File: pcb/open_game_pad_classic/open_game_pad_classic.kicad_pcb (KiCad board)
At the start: 2 copper layers, 140 x 71 mm, 55 parts, among them J1 COM-09032, J2 COM-09032

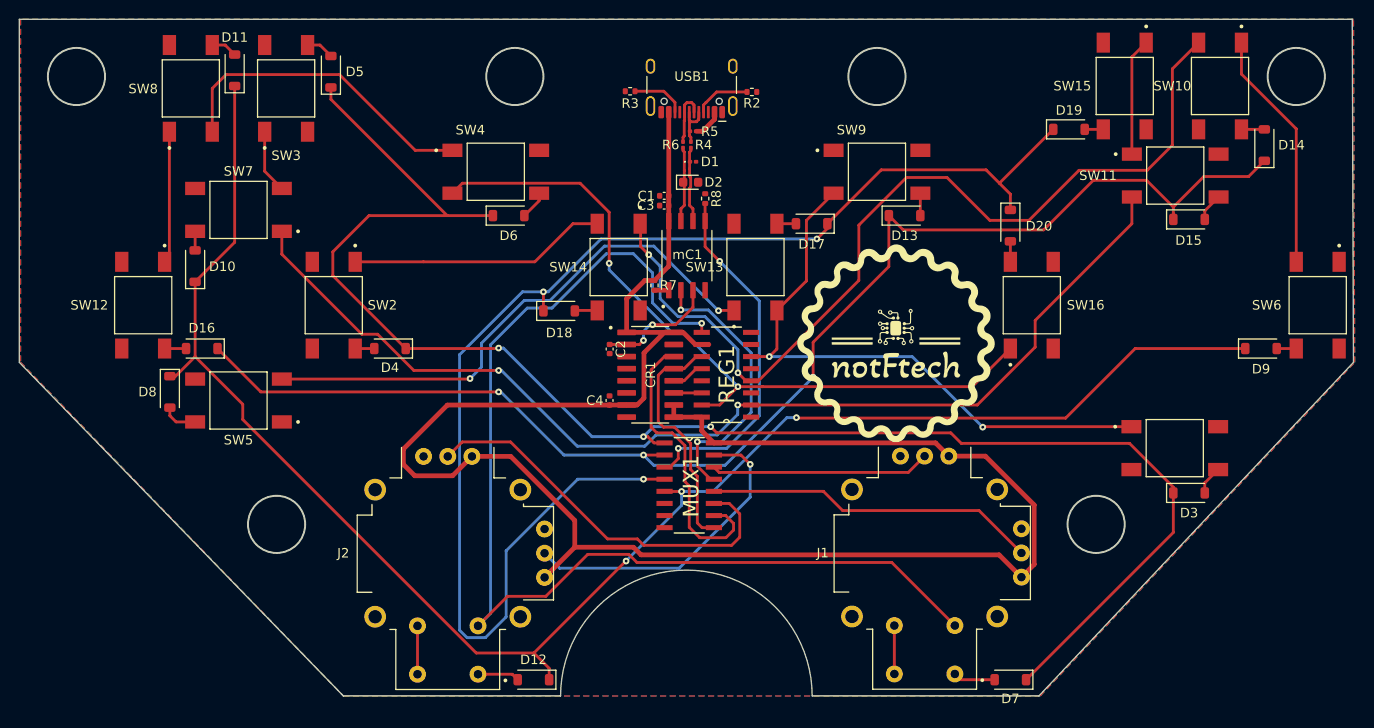
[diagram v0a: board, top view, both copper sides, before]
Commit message: Fixed the switches connections and remade the tracks in pcb.
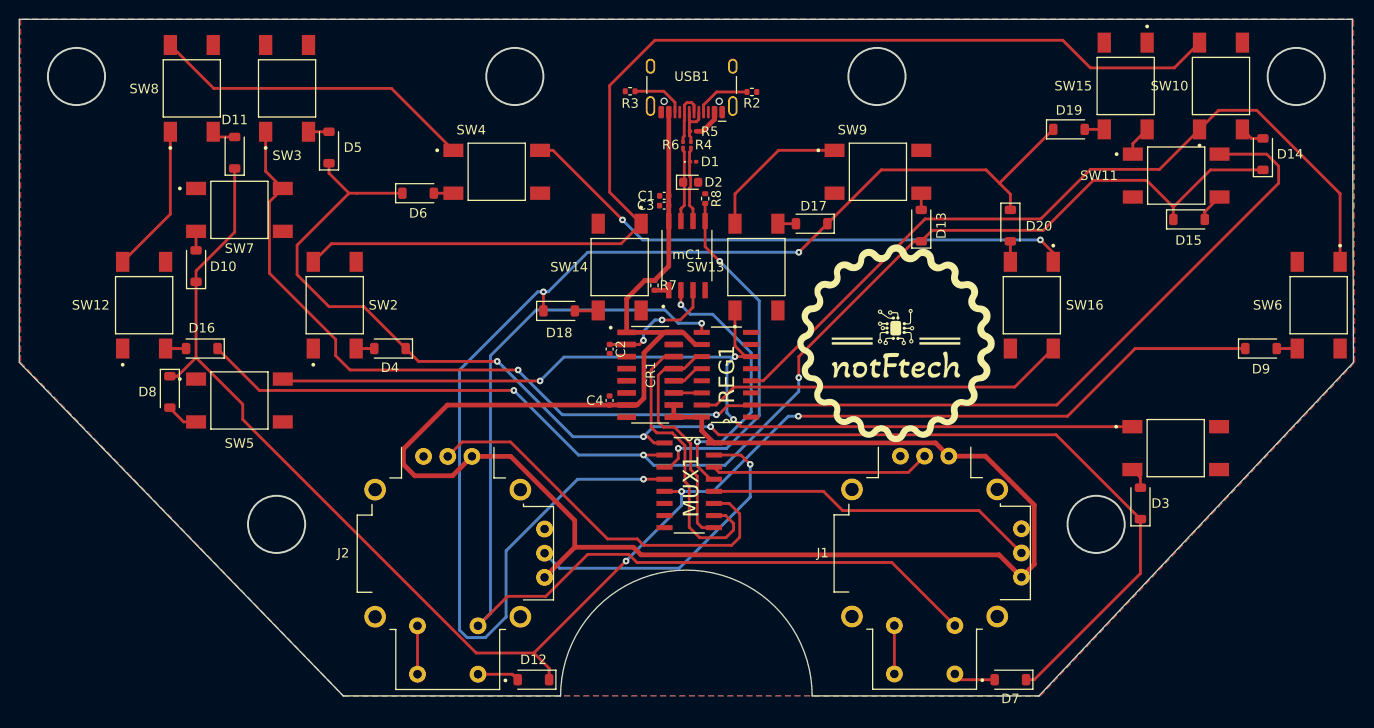
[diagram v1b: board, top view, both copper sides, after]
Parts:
- SW1: value ~ -> TS04-66-95-BK-100-SMT
- moved D6 9.79 mm to (116.8, 72.2)
- moved D11 8.65 mm to (97.6, 68.0)
- moved D5 7.95 mm to (107.5, 67.5)
- moved D3 5.22 mm to (192.7, 104.8), turned to 90 degrees
- moved D13 2.04 mm to (169.7, 75.7), turned to 90 degrees
- moved D14 0.96 mm to (205.5, 68.2)
- moved D10 0.10 mm to (93.5, 79.9)
- moved SW1 0.10 mm to (196.3, 99.0)
- moved SW10 0.10 mm to (201.1, 61.0), turned to 90 degrees
- moved SW11 0.10 mm to (196.4, 70.4)
- moved SW12 0.10 mm to (88.1, 84.0), turned to 90 degrees
- moved SW13 0.10 mm to (152.3, 80.0)
- moved SW14 0.10 mm to (138.0, 80.0)
- moved SW15 0.10 mm to (191.1, 61.0)
- moved SW2 0.10 mm to (108.1, 84.0), turned to 90 degrees
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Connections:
- SW1 pad 2: /Y4 -> Net-(D3-A)
- SW1 pad 3: Net-(D3-A) -> /Y4
- SW10 pad 2: /Y3 -> Net-(D14-A)
- SW10 pad 3: Net-(D14-A) -> /Y3
- SW11 pad 2: /Y2 -> Net-(D15-A)
- SW11 pad 3: Net-(D15-A) -> /Y2
- SW12 pad 2: /Y1 -> Net-(D16-A)
- SW12 pad 3: Net-(D16-A) -> /Y1
- SW13 pad 2: /Y4 -> Net-(D17-A)
- SW13 pad 3: Net-(D17-A) -> /Y4
- SW14 pad 2: /Y3 -> Net-(D18-A)
- SW14 pad 3: Net-(D18-A) -> /Y3
- SW15 pad 2: /Y2 -> Net-(D19-A)
- SW15 pad 3: Net-(D19-A) -> /Y2
- SW16 pad 2: /Y1 -> Net-(D20-A)
- SW16 pad 3: Net-(D20-A) -> /Y1
- SW2 pad 2: /Y3 -> Net-(D4-A)
- SW2 pad 3: Net-(D4-A) -> /Y3
- SW3 pad 2: /Y2 -> Net-(D5-A)
- SW3 pad 3: Net-(D5-A) -> /Y2
- SW4 pad 2: /Y1 -> Net-(D6-A)
- SW4 pad 3: Net-(D6-A) -> /Y1
- SW5 pad 2: /Y4 -> Net-(D8-A)
- SW5 pad 3: Net-(D8-A) -> /Y4
- SW6 pad 2: /Y3 -> Net-(D9-A)
- SW6 pad 3: Net-(D9-A) -> /Y3
- SW7 pad 2: /Y2 -> Net-(D10-A)
- SW7 pad 3: Net-(D10-A) -> /Y2
- SW8 pad 2: /Y1 -> Net-(D11-A)
- SW8 pad 3: Net-(D11-A) -> /Y1
- SW9 pad 2: /Y4 -> Net-(D13-A)
- SW9 pad 3: Net-(D13-A) -> /Y4
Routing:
- net /Y3: track 149.2 -> 202.4 mm, vias 2 -> 0
- net /Y1: track 125.1 -> 148.6 mm
- net /X1: track 166.8 -> 145.2 mm
- net /Y2: track 133.7 -> 151.1 mm
- net /X2: track 177.0 -> 168.3 mm
- net /Y5: track 118.2 -> 110.8 mm
- net /X3: track 140.5 -> 135.6 mm
- net /X4: track 140.5 -> 139.3 mm
- net Net-(D6-A): track 2.99 -> 2.05 mm
- net Net-(D3-A): track 3.03 -> 2.25 mm
- net Net-(D5-A): track 2.93 -> 2.15 mm
- net +5V: track 203.2 -> 202.4 mm
- net /Y4: track 120.4 -> 121.1 mm, vias 4 -> 3
- net Net-(D13-A): track 2.35 -> 1.75 mm

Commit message: Updates the PCB according to new schematic.
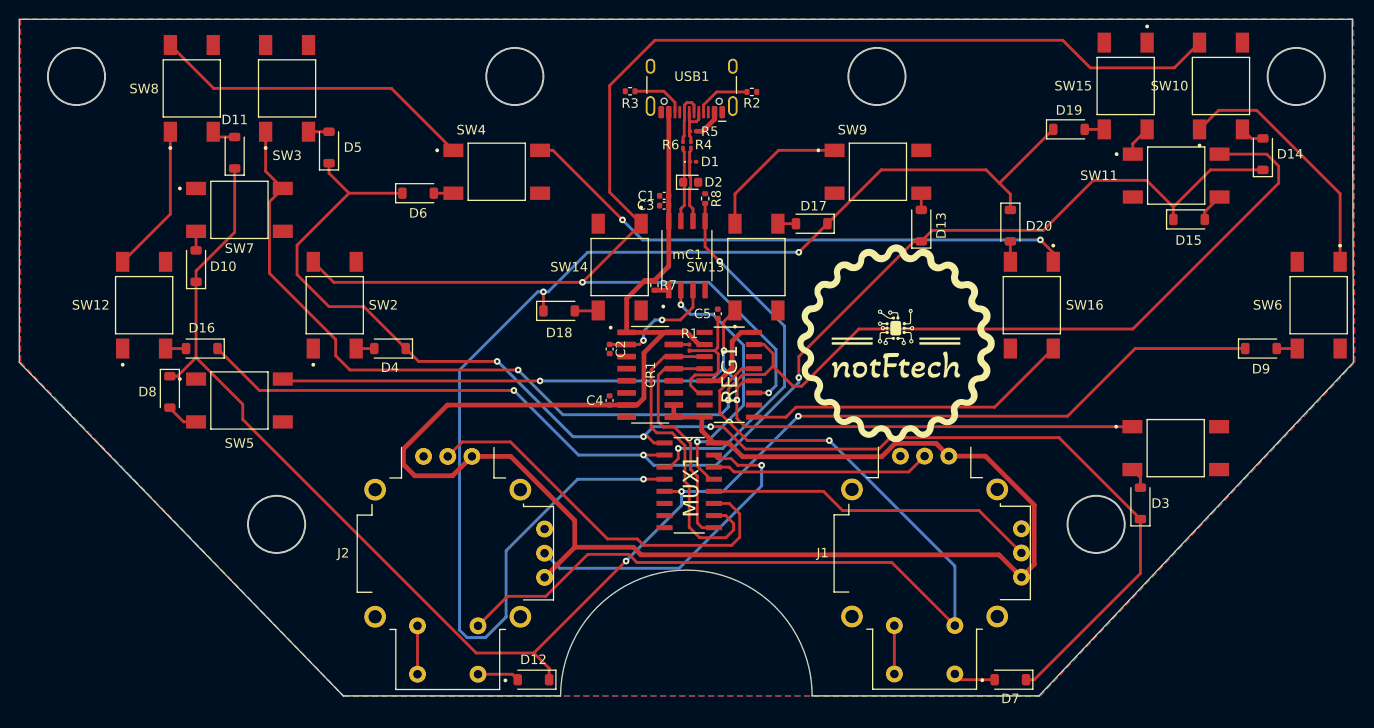
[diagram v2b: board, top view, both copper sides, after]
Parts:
- added C5: 100 pF, Capacitor_SMD:C_0402_1005Metric, F.Cu at (148.3, 84.9)
- added R1: R 1.2 K, Resistor_SMD:R_0201_0603Metric, F.Cu at (145.3, 88.5)
- C2: value 10 pF -> 100 pF
- mC1: value ATtiny85V-20u -> ATtiny85-20su
- moved REG1 0.29 mm to (149.5, 91.3)
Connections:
- CR1 pad 11: /CLK/16 -> unconnected-(CR1-Q3-Pad11)
- CR1 pad 12: /CLK/8 -> unconnected-(CR1-Q2-Pad12)
- CR1 pad 14: Net-(CR1-Q0) -> /CLK/2
- CR1 pad 15: unconnected-(CR1-TC-Pad15) -> /TC
- MUX1 pad 10: Net-(CR1-Q0) -> /CLK/2
- REG1 pad 1: unconnected-(REG1-QB-Pad1) -> /Y1
- REG1 pad 11: /CLK/4 -> /CLK/2
- REG1 pad 12: /CLK/8 -> /CLK/4
- REG1 pad 14: /CLK/16 -> /SEARCH
- REG1 pad 15: /Y1 -> unconnected-(REG1-QA-Pad15)
- REG1 pad 2: /Y2 -> unconnected-(REG1-QC-Pad2)
- REG1 pad 3: unconnected-(REG1-QD-Pad3) -> /Y3
- REG1 pad 4: /Y3 -> /Y4
- REG1 pad 5: unconnected-(REG1-QF-Pad5) -> /Y5
- REG1 pad 6: /Y4 -> unconnected-(REG1-QG-Pad6)
- REG1 pad 7: unconnected-(REG1-QH-Pad7) -> /Y2
- REG1 pad 9: /Y5 -> unconnected-(REG1-QH'-Pad9)
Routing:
- net /CLK/2: track 0.00 -> 33.8 mm
- net Net-(CR1-Q0): track 30.6 -> 0.00 mm
- net /Y3: track 202.4 -> 175.9 mm, vias 0 -> 2
- net /SEARCH: track 0.00 -> 14.2 mm
- net /Y5: track 110.8 -> 100.7 mm
- net GND: track 0.00 -> 8.93 mm
- net /Y2: track 151.1 -> 157.6 mm
- net /Y1: track 148.6 -> 143.6 mm
- net /CLK/8: track 3.46 -> 0.00 mm
- net /CLK/16: track 2.93 -> 0.00 mm
- net +5V: track 202.4 -> 204.8 mm
- net /AIN: track 29.0 -> 27.1 mm
- net /TC: track 0.00 -> 1.65 mm
- net Net-(J2-V): track 33.0 -> 34.6 mm
- net /DIN: track 37.4 -> 38.8 mm
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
